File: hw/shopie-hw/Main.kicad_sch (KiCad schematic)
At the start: 41 parts, among them J1 Jack-DC, J2 USB_B_Micro, J3 Conn_01x04_Socket, SW1 SW_SPDT, SW2 SW_MEC_5E, SW3 SW_SPDT, U2 STM32F405RGT6, U3 LM2596T-5, U4 AP2112K-3.3, U6 MIC5365-1.8YC5, Y2 Crystal_Small

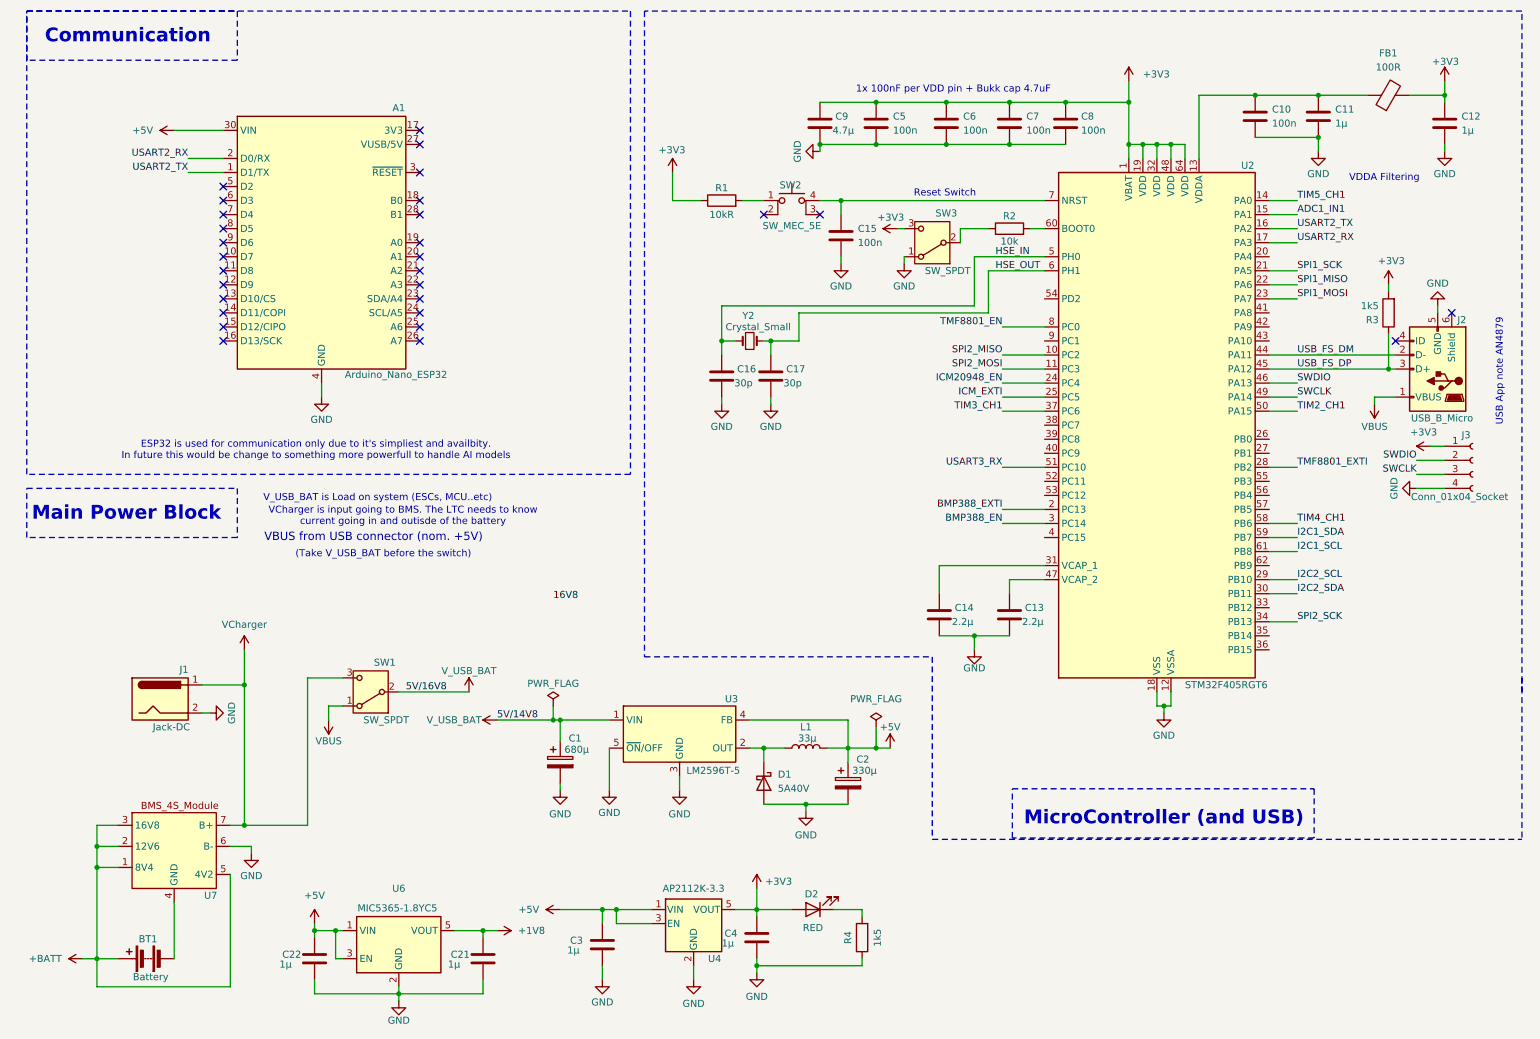
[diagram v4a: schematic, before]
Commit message: Add MOSFET for high-power path separation, isolate ESCs from MCU/sensor rail
- Added BSC016N06NS N-channel MOSFET to control high-current ESC power rail
- Connected MOSFET source to BMS output before switch, drain to ESCs
- Added gate control path to switch MOSFET via GPIO (MCU)
- Added pull-down resistor on gate of MOSFET
- Separated ESC/motor power rail from MCU and sensors
- Prepared schematic for future addition of appropriate fuses
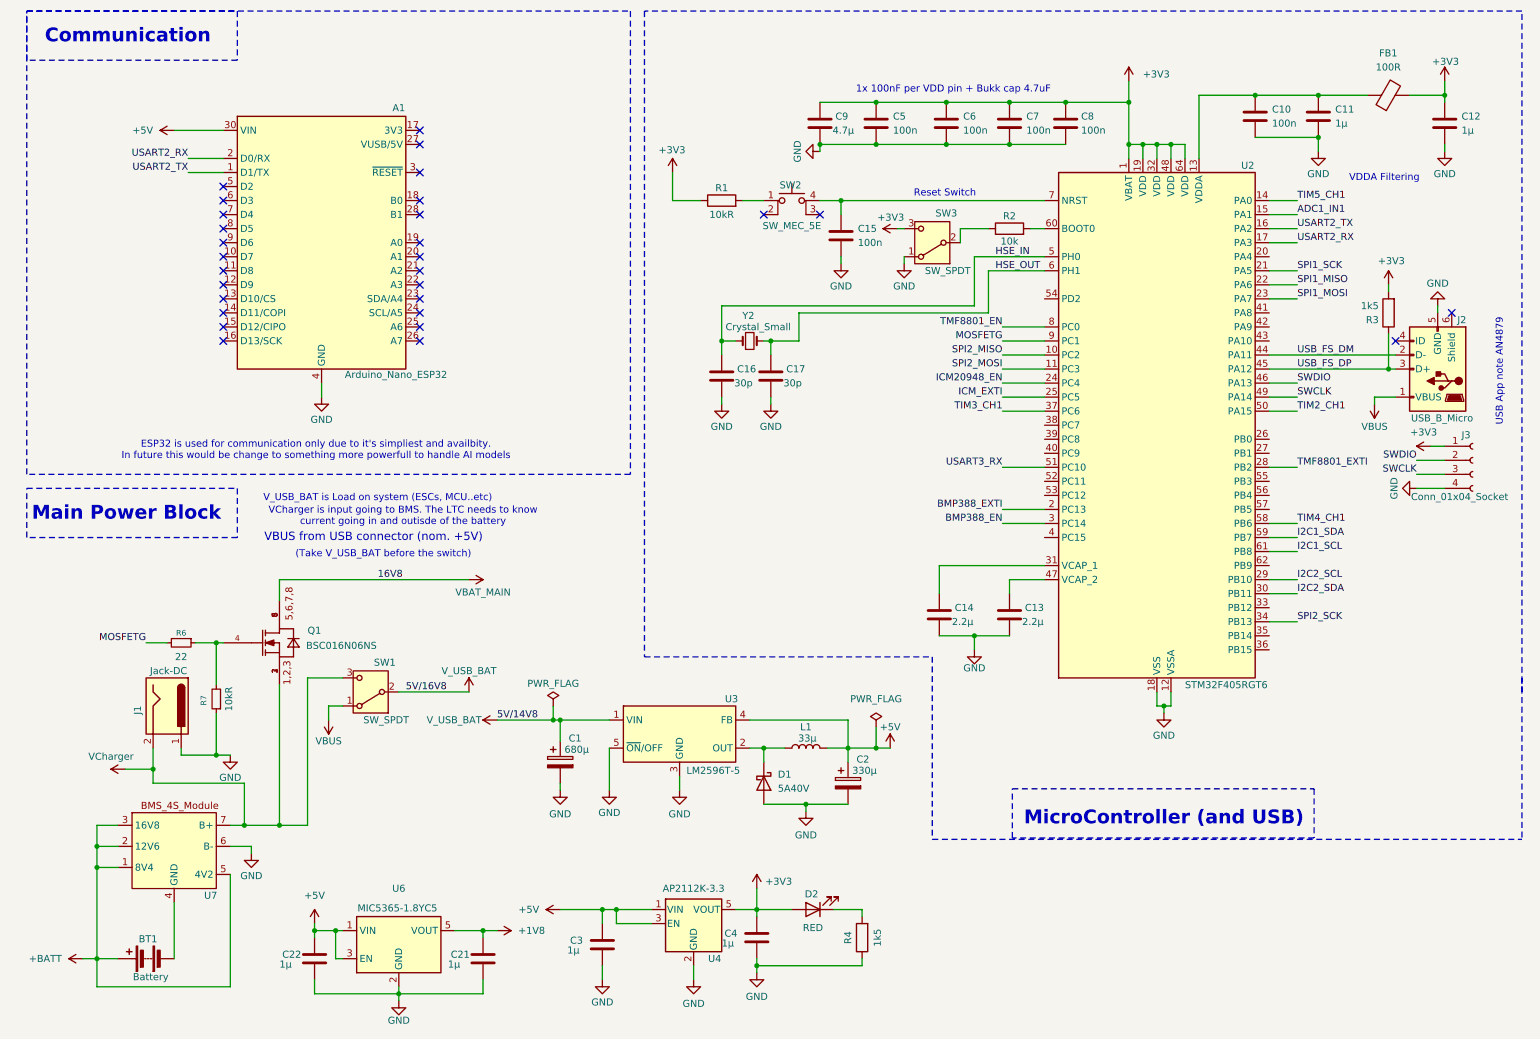
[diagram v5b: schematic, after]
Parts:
- added Q1: BSC016N06NS, BSC016N06NS:INF-PG-TDSON-8-FL, symbol shopie-hwLibrary:BSC016N06NS
- added R6: 22, symbol Device:R_Small
- added R7: 10kR, symbol Device:R_Small
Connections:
- net GND: now also J1.1, R7.1; no longer J1.2
- net VCharger: now also J1.2, Q1.1, Q1.2, Q1.3; no longer J1.1
- net MOSFETG: now reaches U2.9 (PC1)
- net MOSFETG: now also R6.2
- new net: Q1.4, R6.1, R7.2
- new net VBAT_MAIN: Q1.5, Q1.6, Q1.7, Q1.8
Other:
- moved on the sheet: J1

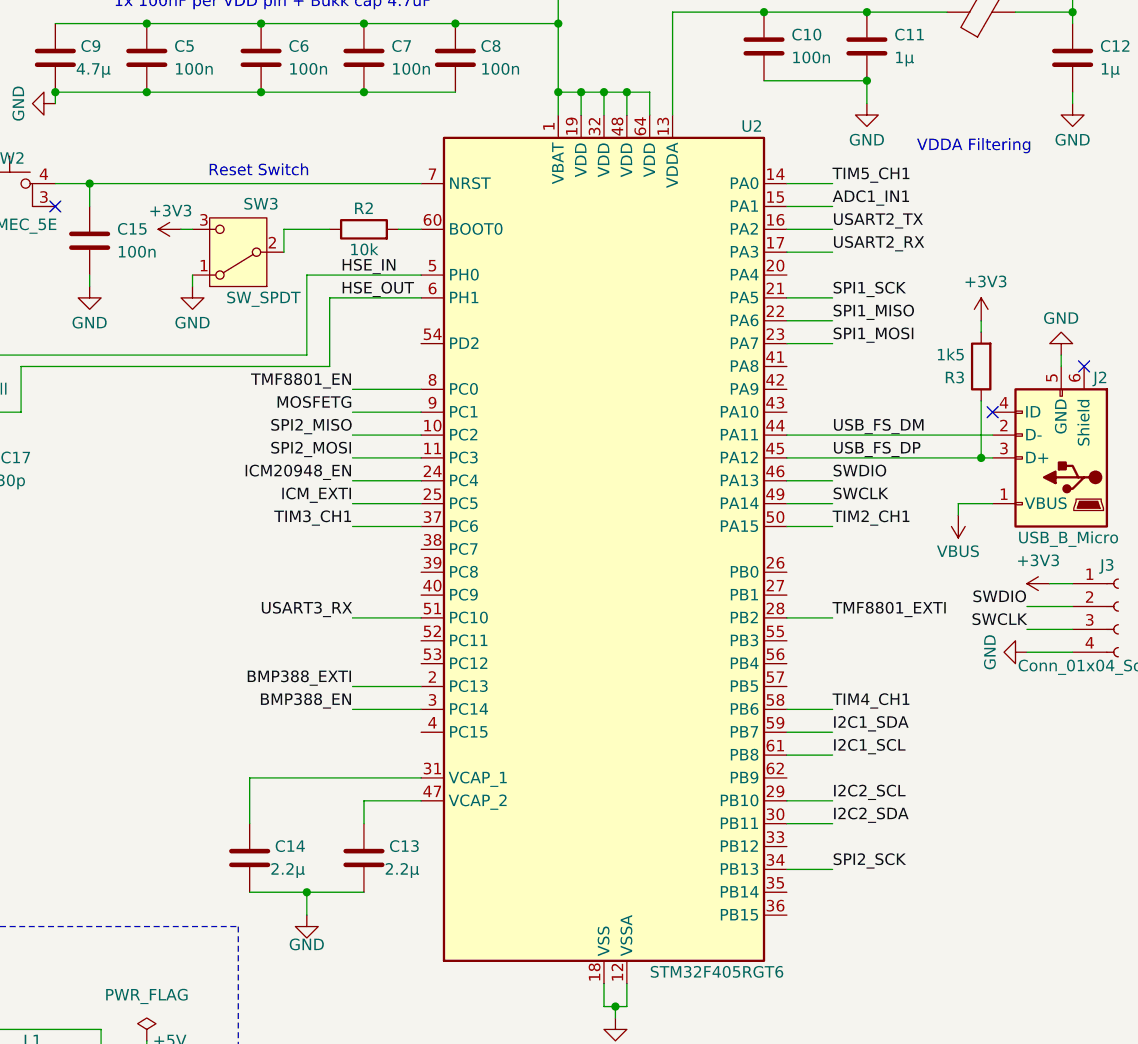
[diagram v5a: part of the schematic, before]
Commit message: Fix most ERC Errors and Connect hierarchical labels across schematic pages
- Connected missing net labels across MCU, Sensors, and Power pages
- Final ERC check passed with no errors or warnings for all labels
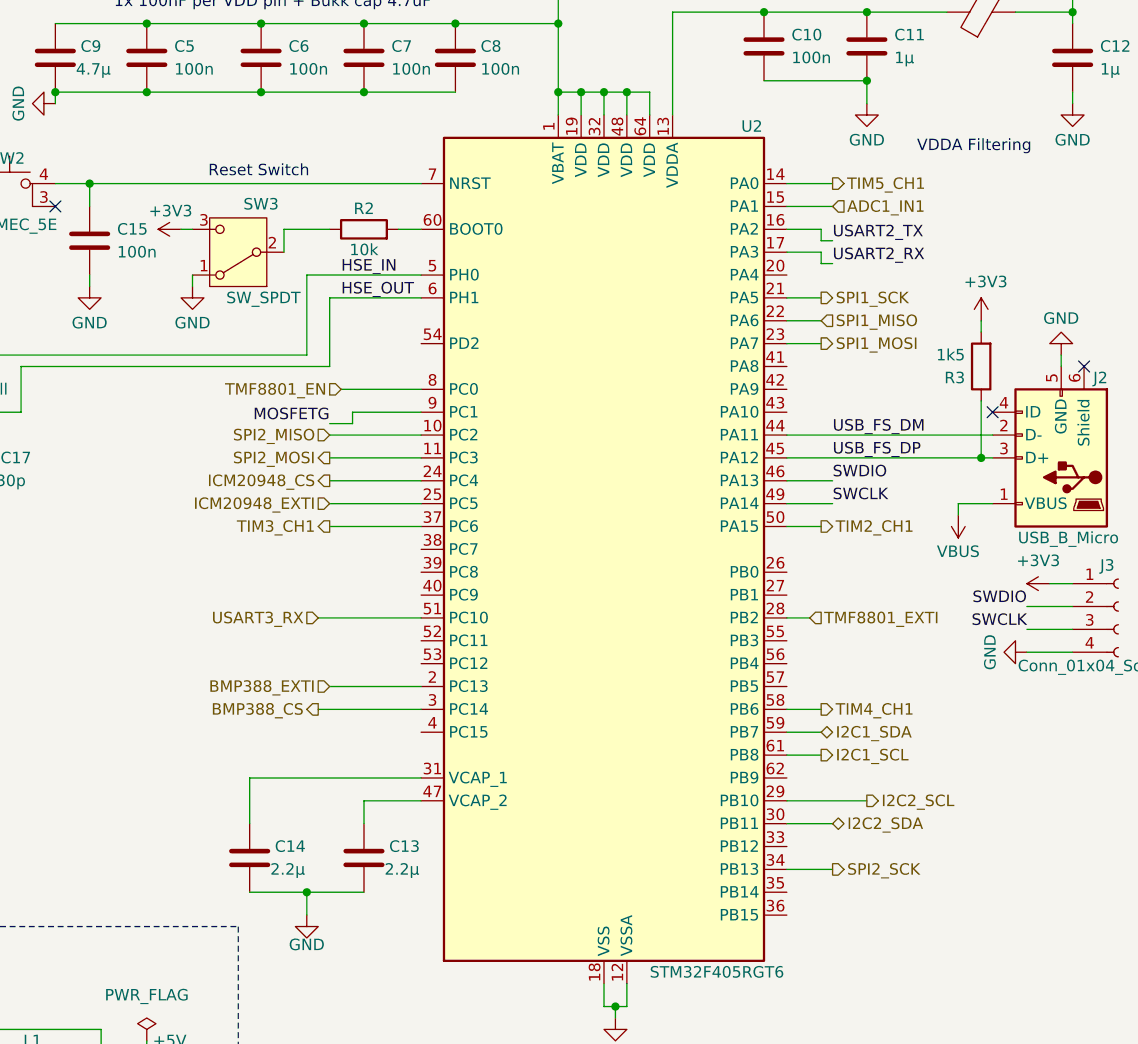
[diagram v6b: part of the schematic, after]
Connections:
- net BMP388_EN renamed BMP388_CS
- net ICM20948_EN renamed ICM20948_CS
- net ICM_EXTI renamed ICM20948_EXTI
